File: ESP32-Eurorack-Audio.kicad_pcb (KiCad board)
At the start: 4 copper layers, 100 x 100 mm, 195 parts, among them J302 USB_B_Micro, J402 Micro_SD_Card, J601 PWR, J701 AUEXT, J702 RIN, J703 LIN/MONO, J704 ROUT, J705 LOUT, J801 TRG0, J802 CVIN1, J803 CVIN3, J804 CVIN2, J805 CVIN4, J806 TRG1, J807 CVIN4, J808 CVIN4, J809 CVIN4, J810 CVIN4, Q201 BSS138, Q202 BSS138, Q301 SS8050-G, Q302 SS8050-G, Q303 SS8050-G, Q801 Q_NPN_BEC, Q802 Q_NPN_BEC, SW201 EN, SW203 FLASH, SW501 SEL, SW801 TRG0, SW802 TRG1, U201 ESP32-WROVER, U301 CP2102N-A01-GQFN24, U601 LM1117-3.3, U602 ADP7118, U701 WM8731, U702 TL074, U801 MCP6004, U802 MCP6004, U803 MCP3208, Y701 11.289600MHz

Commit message: current
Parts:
- removed the G*** at (166.3, 91.4)
- removed TP801: TA, TestPoint:TestPoint_Keystone_5019_Minature
- removed TP802: TB, TestPoint:TestPoint_Keystone_5019_Minature
- removed TP803: TC, TestPoint:TestPoint_Keystone_5019_Minature
- added C503: 100n, Capacitor_SMD:C_0603_1608Metric, F.Cu at (172.1, 68.0)
- added C504: 100n, Capacitor_SMD:C_0603_1608Metric, F.Cu at (167.1, 68.0)
- added C608: 1000u, Capacitor_SMD:CP_Elec_10x12.6, F.Cu at (162.5, 75.8)
- added G***: ctag-logo, specific:ctag-logo, B.Cu at (116.6, 59.4)
- added R603: 10, Resistor_SMD:R_2512_6332Metric, F.Cu at (171.4, 77.6)
- added TP601: 3V3D, TestPoint:TestPoint_Keystone_5019_Minature, B.Cu at (148.5, 66.5)
- added U202: MIC803, Package_TO_SOT_SMD:SOT-23, F.Cu at (165.9, 47.1)
- C202: value 3.3u -> 1u
- D604: footprint LED_SMD:LED_1206_3216Metric_Castellated -> LED_THT:LED_D5.0mm_Clear
- J808: value CVIN4 -> CVIN5
- J809: value CVIN4 -> CVIN6
- J810: value CVIN4 -> CVIN7
- L301: value 600 -> 0
- R302, R305, R306: value 100k -> 10k
- R801, R814: value 10k -> 0
- U601: value LM1117-3.3 -> R-78E3.3-1.0; footprint Package_TO_SOT_SMD:TO-252-2 -> Package_SIP:SIP3_11.6x8.5mm; moved to B.Cu
- moved U601 10.6 mm to (158.2, 68.8), turned to 0 degrees
- moved R602 6.81 mm to (170.9, 72.2)
- moved D604 1.35 mm to (169.3, 70.0), turned to 0 degrees
- moved JP201 0.46 mm to (162.3, 51.1)
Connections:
- J702 pad 2: Net-(J702-Pad2) -> GND
- J703 pad 1: Net-(J702-Pad2) -> Net-(J703-Pad1)
- R706 pad 2: Net-(J702-Pad2) -> Net-(J703-Pad1)
- R824 pad 2: Net-(J808-Pad1) -> Net-(J809-Pad1)
- R829 pad 2: Net-(J809-Pad1) -> Net-(J808-Pad1)
- U601 pad 1: GND -> Net-(C608-Pad1)
- U601 pad 2: +3V3 -> GND
- U601 pad 3: Net-(C606-Pad1) -> +3V3
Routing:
- net +3V3: track 202.5 -> 153.2 mm, vias 47 -> 33
- net Net-(J702-Pad2): track 24.4 -> 0.00 mm
- net Net-(C608-Pad1): track 0.00 -> 19.6 mm
- net GND: track 395.0 -> 413.0 mm, vias 302 -> 306
- net Net-(J703-Pad1): track 0.00 -> 12.3 mm
- net /ESP-main/IO12: track 112.1 -> 103.0 mm
- net /ESP-main/IO32: track 88.6 -> 83.2 mm
- net Net-(J808-Pad1): track 2.42 -> 7.22 mm
- net /ESP-main/EN: track 78.2 -> 82.1 mm, vias 2 -> 3
- net /ESP-main/IO13: track 110.7 -> 107.2 mm
- net +3.3VA: track 76.1 -> 79.4 mm
- net Net-(J809-Pad1): track 28.0 -> 29.6 mm
- net /UI/ENC_B: track 68.3 -> 69.6 mm
- net /UI/ENC_A: track 62.9 -> 64.2 mm
- net Net-(C606-Pad1): track 77.6 -> 76.6 mm
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- removed copper zone on F.Cu, net +3V3
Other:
- board text added: "ESP-Audio Rev. C2 (c) R. Manzke 2019"
- board text removed: "ESP-Audio Rev. B2 (c) R. Manzke 2018"

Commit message: PCB and BOM updated, cleanups
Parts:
- removed C204: 1n, Capacitor_SMD:C_0603_1608Metric
- removed D301: STPS2L40ZFY, Diode_SMD:D_SOD-123
- removed D302, D401, D402: SP0503BAHT, Package_TO_SOT_SMD:SOT-143
- removed FID1, FID2, FID3: ~, Fiducial:Fiducial_1mm_Dia_2.54mm_Outer_CopperTop
- removed the G*** at (116.6, 59.4)
- removed JP201, JP202: Jumper, Jumper:SolderJumper-2_P1.3mm_Open_TrianglePad1.0x1.5mm
- removed JP601: VSEL, Connector_PinHeader_2.54mm:PinHeader_1x03_P2.54mm_Vertical
- removed L301: 0, Capacitor_SMD:C_0805_2012Metric
- removed Q201, Q202: BSS138, Package_TO_SOT_SMD:SOT-23
- removed R202, R204: 1k, Resistor_SMD:R_0603_1608Metric
- removed R203: 10k, Resistor_SMD:R_0603_1608Metric
- removed R801, R814: 0, Resistor_SMD:R_0603_1608Metric
- removed SW201: EN, Button_Switch_SMD:SW_SPST_PTS810
- removed SW203: FLASH, Button_Switch_SMD:SW_SPST_PTS810
- removed TP301: TP_EN, TestPoint:TestPoint_Keystone_5019_Minature
- removed TP302: TP_IO0, TestPoint:TestPoint_Keystone_5019_Minature
- removed TP303: TP_IO2, TestPoint:TestPoint_Keystone_5019_Minature
- removed TP304: TP_RXD, TestPoint:TestPoint_Keystone_5019_Minature
- removed TP305: TP_TXD, TestPoint:TestPoint_Keystone_5019_Minature
- removed TP306: TP_DTR, TestPoint:TestPoint_Keystone_5019_Minature
- removed TP307: TP_RTS, TestPoint:TestPoint_Keystone_5019_Minature
- removed TP601: 3V3D, TestPoint:TestPoint_Keystone_5019_Minature
- removed TP602: TestPoint, TestPoint:TestPoint_Keystone_5019_Minature
- added C505: 100n, Capacitor_SMD:C_0603_1608Metric, F.Cu at (170.3, 48.5)
- added G***: ctag-logo-sm, specific:ctag-logo-sm, B.Cu at (166.4, 91.3)
- added G***: ctag-logo-sm, specific:ctag-logo-sm, F.Cu at (136.7, 79.7)
- D604: value APTD3216SURCK -> ~
- moved R404 7.76 mm to (105.2, 52.0)
- moved TP101 2.69 mm to (97.8, 73.8)
- moved JP101 1.74 mm to (94.3, 69.3)
- moved C807 1.50 mm to (108.7, 64.9)
- moved R503 0.28 mm to (171.9, 47.0)
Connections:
- C606 pad 1: Net-(C606-Pad1) -> +12V
- J302 pad 4: Net-(J302-Pad4) -> (no net)
- J302 pad 5: Net-(J302-Pad5) -> GND
- J302 pad 6: Net-(J302-Pad5) -> GND
- J402 pad 1: /SD/DAT2 -> (no net)
- J402 pad 8: /SD/DAT1 -> (no net)
- J704 pad 2: Net-(J704-Pad2) -> (no net)
- J705 pad 2: Net-(J705-Pad2) -> (no net)
- Q801 pad 3: Net-(Q801-Pad3) -> /GATE_CV/TRG0
- Q802 pad 3: Net-(Q802-Pad3) -> /GATE_CV/TRG1
- R603 pad 2: Net-(C606-Pad1) -> +12V
- R802 pad 1: Net-(Q801-Pad3) -> /GATE_CV/TRG0
- R817 pad 1: Net-(Q802-Pad3) -> /GATE_CV/TRG1
- SW801 pad 1: Net-(Q801-Pad3) -> /GATE_CV/TRG0
- SW802 pad 1: Net-(Q802-Pad3) -> /GATE_CV/TRG1
- U201 pad 17: Net-(U201-Pad17) -> (no net)
- U201 pad 18: Net-(U201-Pad18) -> (no net)
- U201 pad 19: Net-(U201-Pad19) -> (no net)
- U201 pad 20: Net-(U201-Pad20) -> (no net)
- U201 pad 21: Net-(U201-Pad21) -> (no net)
- U201 pad 22: Net-(U201-Pad22) -> (no net)
- U201 pad 27: Net-(U201-Pad27) -> (no net)
- U201 pad 28: Net-(U201-Pad28) -> (no net)
- U201 pad 32: Net-(U201-Pad32) -> (no net)
- U301 pad 1: Net-(U301-Pad1) -> (no net)
- U301 pad 10: Net-(U301-Pad10) -> (no net)
- U301 pad 11: Net-(U301-Pad11) -> (no net)
- U301 pad 12: Net-(U301-Pad12) -> (no net)
- U301 pad 13: Net-(U301-Pad13) -> (no net)
- U301 pad 14: Net-(U301-Pad14) -> (no net)
- U301 pad 15: Net-(U301-Pad15) -> (no net)
- U301 pad 16: Net-(U301-Pad16) -> (no net)
- U301 pad 17: Net-(U301-Pad17) -> (no net)
- U301 pad 18: Net-(U301-Pad18) -> (no net)
- U301 pad 22: Net-(U301-Pad22) -> (no net)
- U301 pad 24: Net-(U301-Pad24) -> (no net)
- U602 pad 1: Net-(C606-Pad1) -> +12V
- U602 pad 3: Net-(C606-Pad1) -> +12V
- U701 pad 2: Net-(U701-Pad2) -> (no net)
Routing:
- net +12V: track 158.6 -> 247.1 mm, vias 3 -> 10
- net Net-(C606-Pad1): track 76.6 -> 0.00 mm, vias 5 -> 0
- net /GATE_CV/TRG1: track 46.0 -> 119.0 mm, vias 2 -> 4
- net Net-(Q802-Pad3): track 72.6 -> 0.00 mm, vias 2 -> 0
- net Net-(Q801-Pad3): track 64.1 -> 0.00 mm, vias 2 -> 0
- net /GATE_CV/TRG0: track 27.4 -> 88.8 mm, vias 2 -> 4
- net Net-(C204-Pad1): track 45.2 -> 2.23 mm
- net /ESP-main/EN: track 82.1 -> 53.0 mm
- net /SD/DAT1: track 27.8 -> 0.00 mm, vias 2 -> 0
- net +3V3: track 153.2 -> 125.5 mm, vias 33 -> 31
- net GND: track 413.0 -> 387.3 mm, vias 306 -> 303
- net Net-(J302-Pad1): track 31.1 -> 5.80 mm, vias 2 -> 0
- net /USB/EXT_5V: track 24.7 -> 0.00 mm
- net /USB/RTS: track 41.3 -> 22.5 mm, vias 5 -> 4
- net /SD/DAT2: track 16.7 -> 0.00 mm, vias 2 -> 0
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- added copper zone on F.Cu, net +12V
- removed copper zone on F.Cu, net Net-(C606-Pad1)
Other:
- board text added: "ESP-Audio Rev. D (c) R. Manzke 2019"
- board text removed: "ESP-Audio Rev. C2 (c) R. Manzke 2019"

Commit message: cleanups and gerbers
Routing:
- net GND: track 387.3 -> 399.7 mm
- net /SD/D0: track 100.7 -> 97.7 mm
- net Net-(C204-Pad1): track 2.23 -> 0.00 mm
- net /SD/CLK: track 65.5 -> 65.0 mm

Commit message: sending for production
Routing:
- net GND: track 399.7 -> 446.7 mm
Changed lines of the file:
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@@
     (thickness 1.6)
     (drawings 83)
-    (tracks 2502)
+    (tracks 2511)
     (zones 0)
     (modules 170)
@@
     (38 B.Mask user)
     (39 F.Mask user)
-    (40 Dwgs.User user hide)
+    (40 Dwgs.User user)
     (41 Cmts.User user hide)
     (42 Eco1.User user hide)
@@
     (pad_drill 0.762)
     (pad_to_mask_clearance 0)
-    (pad_to_paste_clearance -0.0635)
+    (pad_to_paste_clearance -0.0762)
     (aux_axis_origin 86.85 135.15)
     (grid_origin 86.85 135.15)
@@
   (segment (start 180.6 79.65) (end 179.6 80.65) (width 1.143) (layer B.Cu) (net 104))
   (segment (start 180.6 78.65) (end 180.6 79.65) (width 1.143) (layer B.Cu) (net 104))
+  (segment (start 181.85 61.53) (end 181.85 66.61) (width 1.143) (layer In1.Cu) (net 104))
+  (segment (start 184.39 61.53) (end 184.39 66.61) (width 1.143) (layer In1.Cu) (net 104))
+  (segment (start 181.85 61.53) (end 184.39 61.53) (width 1.143) (layer In1.Cu) (net 104))
+  (segment (start 181.85 66.61) (end 184.39 66.61) (width 1.143) (layer In1.Cu) (net 104))
+  (segment (start 181.85 64.07) (end 184.39 64.07) (width 1.143) (layer In1.Cu) (net 104))
+  (segment (start 183.35 80.60318) (end 183.35 94.15) (width 1.143) (layer In1.Cu) (net 104))
+  (segment (start 185.96334 77.98984) (end 183.35 80.60318) (width 1.143) (layer In1.Cu) (net 104))
+  (segment (start 184.39 66.61) (end 185.96334 68.18334) (width 1.143) (layer In1.Cu) (net 104))
+  (segment (start 185.96334 68.18334) (end 185.96334 77.98984) (width 1.143) (layer In1.Cu) (net 104))
   (via (at 155.6 61.15) (size 0.45) (drill 0.2) (layers F.Cu B.Cu) (net 105))
   (segment (start 148.280077 61.055999) (end 142.85 55.625922) (width 0.254) (layer F.Cu) (net 105))

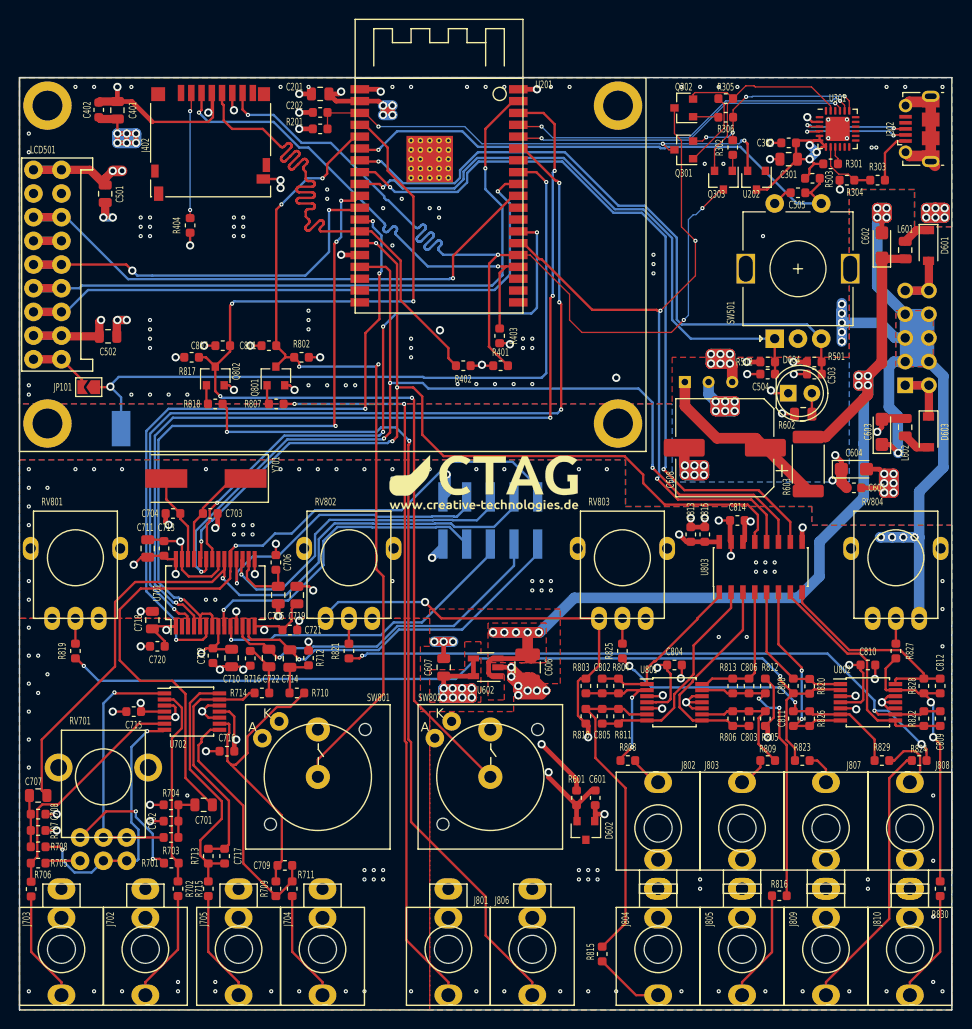
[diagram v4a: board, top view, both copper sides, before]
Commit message: added pcb fiducials, updated date
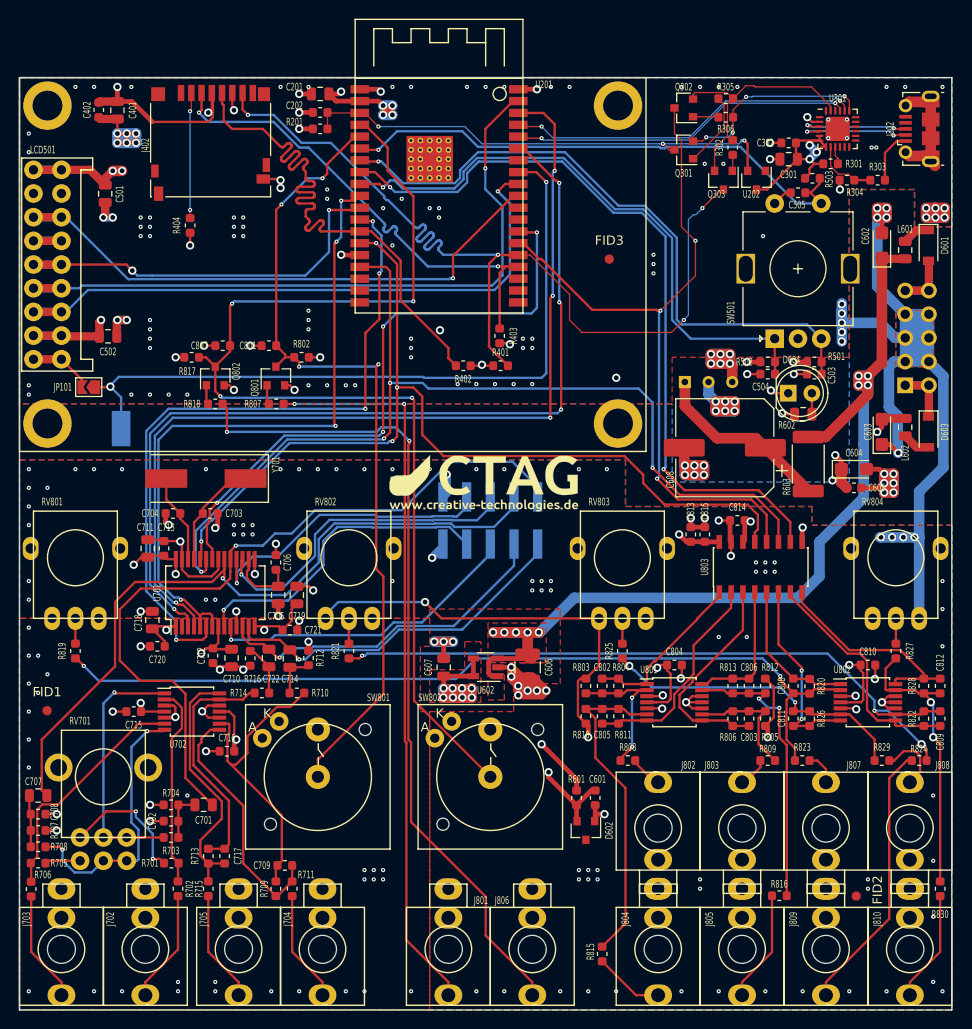
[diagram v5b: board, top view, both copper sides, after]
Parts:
- added FID1: Fiducial, Fiducial:Fiducial_1mm_Mask2mm, F.Cu at (89.8, 104.0)
- added FID2: Fiducial, Fiducial:Fiducial_1mm_Mask2mm, F.Cu at (176.6, 123.9)
- added FID3: Fiducial, Fiducial:Fiducial_1mm_Mask2mm, F.Cu at (150.1, 55.6)
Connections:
- J302 pad 4: (no net) -> Net-(J302-Pad4)
- J402 pad 1: (no net) -> Net-(J402-Pad1)
- J402 pad 8: (no net) -> Net-(J402-Pad8)
- J704 pad 2: (no net) -> Net-(J704-Pad2)
- J705 pad 2: (no net) -> Net-(J705-Pad2)
- U201 pad 17: (no net) -> Net-(U201-Pad17)
- U201 pad 18: (no net) -> Net-(U201-Pad18)
- U201 pad 19: (no net) -> Net-(U201-Pad19)
- U201 pad 20: (no net) -> Net-(U201-Pad20)
- U201 pad 21: (no net) -> Net-(U201-Pad21)
- U201 pad 22: (no net) -> Net-(U201-Pad22)
- U201 pad 27: (no net) -> Net-(U201-Pad27)
- U201 pad 28: (no net) -> Net-(U201-Pad28)
- U201 pad 32: (no net) -> Net-(U201-Pad32)
- U301 pad 1: (no net) -> Net-(U301-Pad1)
- U301 pad 10: (no net) -> Net-(U301-Pad10)
- U301 pad 11: (no net) -> Net-(U301-Pad11)
- U301 pad 12: (no net) -> Net-(U301-Pad12)
- U301 pad 13: (no net) -> Net-(U301-Pad13)
- U301 pad 14: (no net) -> Net-(U301-Pad14)
- U301 pad 15: (no net) -> Net-(U301-Pad15)
- U301 pad 16: (no net) -> Net-(U301-Pad16)
- U301 pad 17: (no net) -> Net-(U301-Pad17)
- U301 pad 18: (no net) -> Net-(U301-Pad18)
- U301 pad 22: (no net) -> Net-(U301-Pad22)
- U301 pad 24: (no net) -> Net-(U301-Pad24)
- U701 pad 2: (no net) -> Net-(U701-Pad2)
